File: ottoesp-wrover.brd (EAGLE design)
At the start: 57.2 x 53.3 mm, 43 parts, among them CN1 Servo, CN2 Servo, CN3 Servo, CN4 Servo, CN5 Servo, CN6 Servo, J1 DC-005, J2 4p-2.54, J3 4p-2.54, Q1 S8050, Q2 S8050, Q3 CJ2302, U1 CJT1117-5.0-SOT223, U2 CP2102, U3 CJA1117B-3.3-SOT89, U4 TPD4S012DRYR

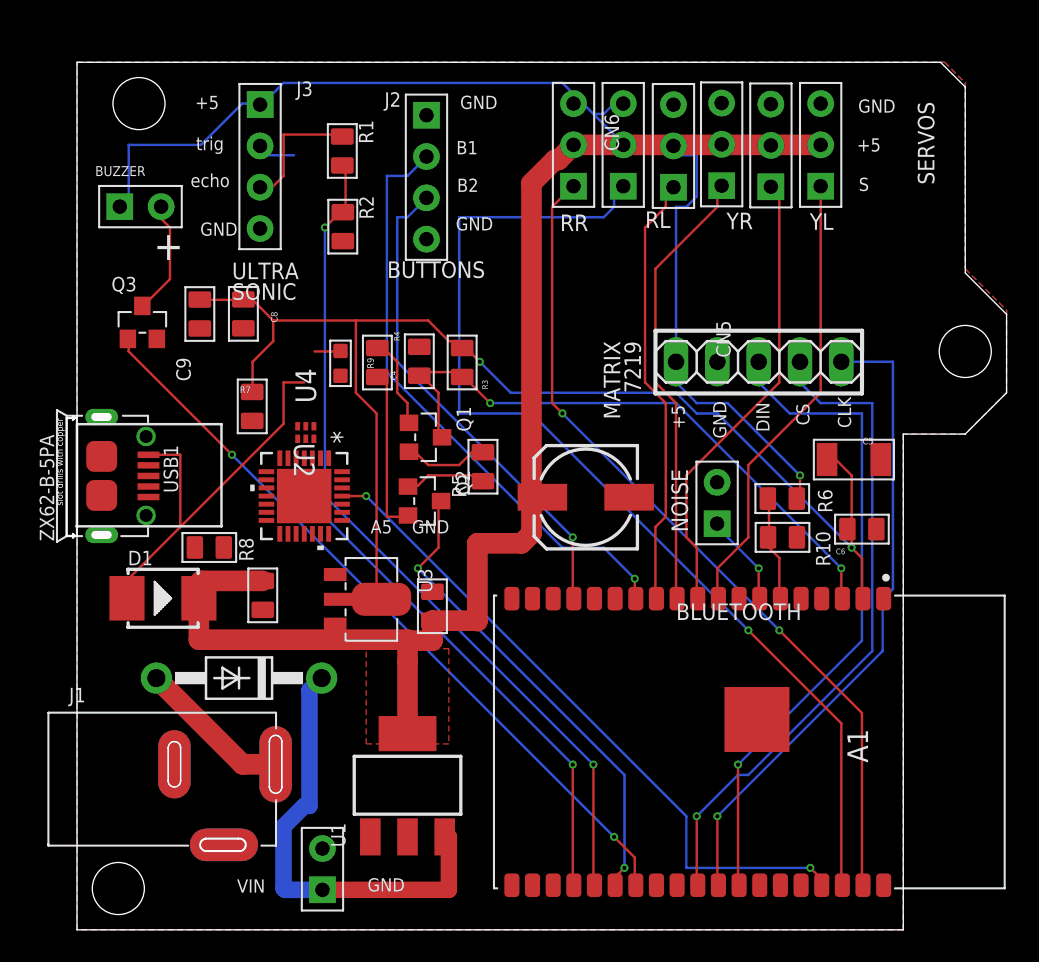
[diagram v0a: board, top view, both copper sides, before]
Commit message: Moved pins to allow a better PCB routing. Fixed all DRC errors.
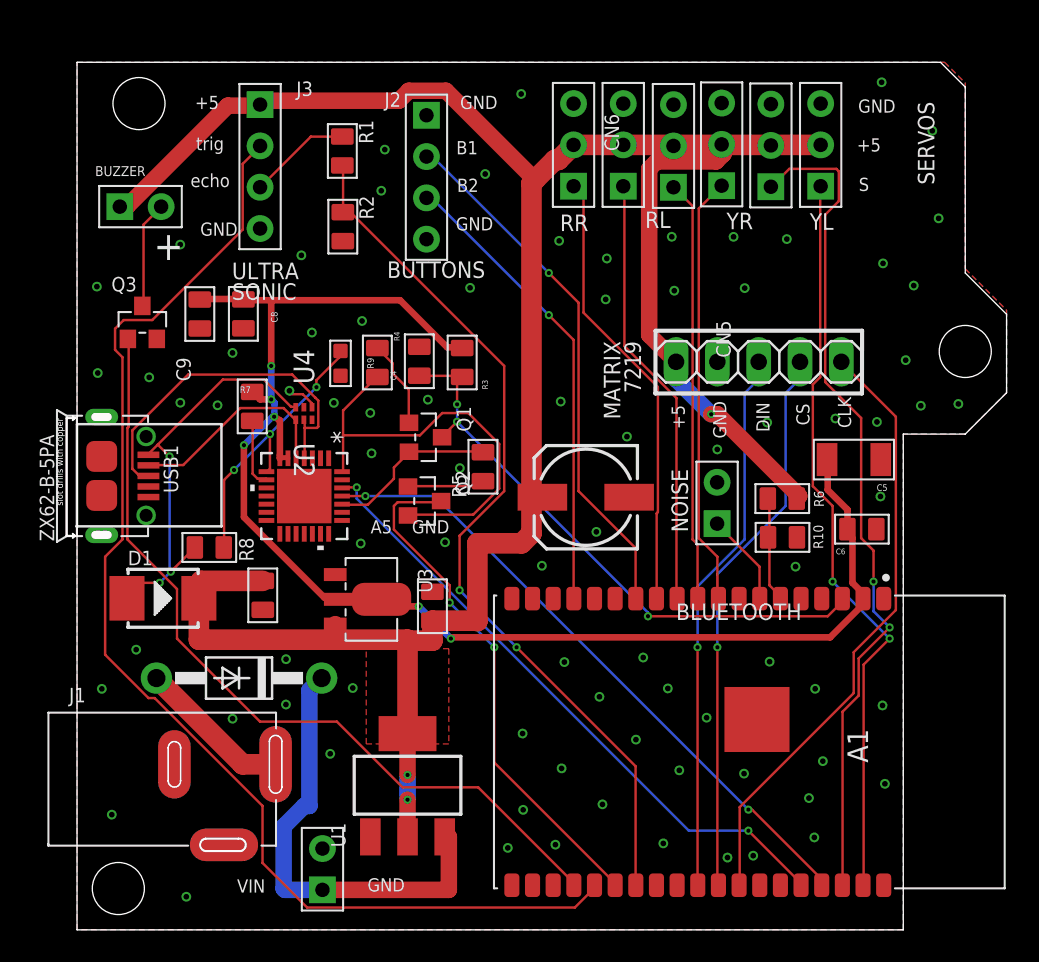
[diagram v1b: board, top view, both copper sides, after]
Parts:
- moved U4 1.17 mm to (24.1, 31.7)
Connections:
- net IO0 renamed BOOT
- net N$1 renamed RXD
- net N$2 renamed TXD
- net BUZZER: now also A1.23; no longer A1.26
- net CLK: now also A1.31; no longer A1.30
- net CS: now also A1.30; no longer A1.29
- net DIN: now also A1.29; no longer A1.31
- net ECHO3.3: now also A1.26; no longer A1.24
- net GND: now also CN5.3, CN6.3, U2.1, U2.2
- net SERVO1: now also A1.37; no longer A1.9
- net SERVO2: now also A1.36; no longer A1.10
- net SERVO3: now also A1.9; no longer A1.11
- net SERVO4: now also A1.10; no longer A1.12
- net SERVO5: now also A1.11; no longer A1.36
- net SERVO6: now also A1.12; no longer A1.37
- net TRIG: now also A1.24; no longer A1.23
- net V+: no longer CN5.3, CN6.3
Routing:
- net TRIG: track 34.2 -> 75.9 mm, vias 1 -> 0
- net RXD: track 0.00 -> 38.9 mm, vias 0 -> 2
- net SERVO5: track 65.0 -> 26.8 mm, vias 1 -> 0
- net SERVO6: track 51.4 -> 27.6 mm, vias 2 -> 0
- net SERVO2: track 28.2 -> 51.8 mm, vias 0 -> 2
- net N$10: track 0.00 -> 21.9 mm
- net SERVO1: track 28.0 -> 45.8 mm, vias 0 -> 2
- net DTR: track 10.3 -> 26.8 mm
- net N$7: track 1.60 -> 17.5 mm, vias 0 -> 3
- net N$8: track 0.00 -> 13.2 mm
- net 3.3V: track 82.0 -> 89.5 mm, vias 2 -> 6
- net DIN: track 40.6 -> 34.2 mm
- net RTS: track 5.69 -> 10.5 mm
- net CS: track 40.7 -> 36.1 mm
- net N$6: track 0.00 -> 4.29 mm
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
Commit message: Updated to use parts I can find at mouser. Used a higher power 3.3V regulator. Added Gerber zip that I used to order prototype boards from SEEED.
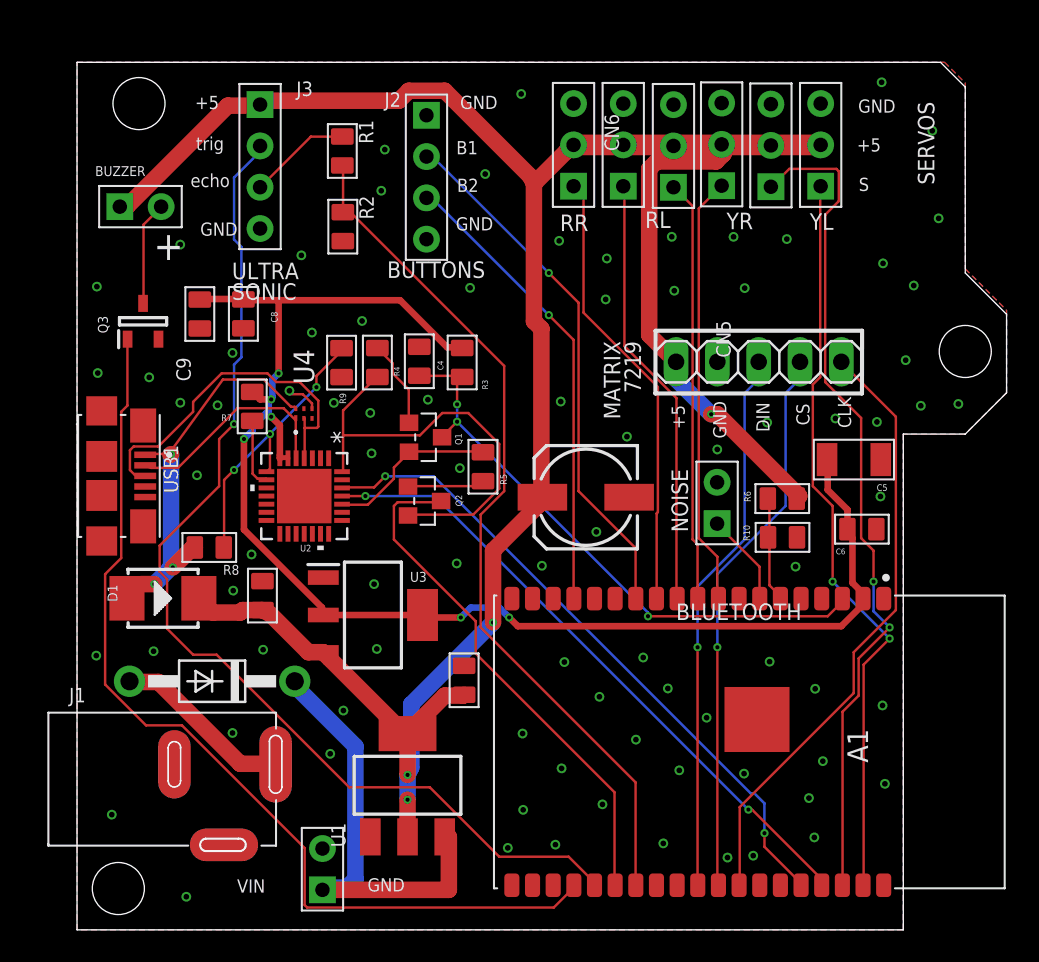
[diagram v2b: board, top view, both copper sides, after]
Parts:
- added FRAME1: FRAME-LEDGERMISHAFARMS, SparkFun-Aesthetics:MISHAFARMS
- Q3: device Seeed-Transistor:SOT-23 -> SamacSys_Parts:SOT95P230X110-3N
- R9: device OPL_Resistor:R0603 -> OPL_Resistor:R0805
- U1: value CJT1117-5.0-SOT223 -> 5.0V REG
- U3: device OPL_IC:SOT-89 -> SamacSys_Parts:SOT230P700X180-4N
- U4: device TPD4S012:DRY6 -> SamacSys_Parts:TPD4S012DRYR
- USB1: device OPL_Connector:MICRO-USB5+6P-SMD-0.65-AB -> XLibrary:HRS_ZX62-B-5PA(33)
- moved C1 4.95 mm to (34.0, 15.3)
- moved DP1 1.67 mm to (18.5, 15.3)
- moved U3 1.05 mm to (28.4, 19.4), turned to 0 degrees
- moved Q3 0.08 mm to (14.2, 37.4), turned to 90 degrees
- moved R9 0.08 mm to (26.4, 34.9)
- turned C3 to 180 degrees
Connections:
- net VBUS renamed N$1
- net GND: now also USB1.SH1, USB1.SH2, USB1.SH3, USB1.SH4, USB1.SH5, USB1.SH6; no longer USB1.P1, USB1.P2, USB1.P3, USB1.P4, USB1.P5, USB1.P6
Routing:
- net TRIG: track 75.9 -> 65.8 mm, vias 0 -> 1
- net BUZZER: track 50.5 -> 59.0 mm
- net V+: track 150.7 -> 147.5 mm, vias 3 -> 4
- net RXD: track 38.9 -> 40.6 mm
- net N$9: track 9.53 -> 11.1 mm
- net ECHO3.3: track 54.3 -> 53.3 mm, vias 2 -> 0
- net 3.3V: track 89.5 -> 90.2 mm
- net N$10: track 21.9 -> 22.5 mm
- net GND: track 2.07 -> 2.16 mm, vias 82 -> 85
- net BOOT: vias 2 -> 0
- removed copper zone on layer 1, net V+
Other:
- board text removed: "A5"

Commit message: .gitignore all the files that eagle creates that we don't want uploaded. Added the BOM in CSV (this is the BOM from Mouser) Changed a 20K resistor to 22K so that we don't need some many different resistors
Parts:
- R2: value 20K -> 22K
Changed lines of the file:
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@@
 <attribute name="VALUE" x="24.565678125" y="49.790540625" size="0.889" layer="27" ratio="11" rot="R270"/>
 </element>
-<element name="R2" library="OPL_Resistor" library_urn="urn:adsk.eagle:library:8004883" package="R0805" package3d_urn="urn:adsk.eagle:package:8004935/1" value="20K" x="26.500446875" y="43.233915625" smashed="yes" rot="R180">
+<element name="R2" library="OPL_Resistor" library_urn="urn:adsk.eagle:library:8004883" package="R0805" package3d_urn="urn:adsk.eagle:package:8004935/1" value="22K" x="26.500446875" y="43.233915625" smashed="yes" rot="R180">
 <attribute name="MPN" value="RC0805JR-071KL" x="26.500446875" y="43.233915625" size="1.778" layer="27" rot="R180" display="off"/>
 <attribute name="NAME" x="27.516446875" y="45.138915625" size="0.889" layer="25" ratio="11" rot="R270"/>

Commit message: The latest schematic and board layout
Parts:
- removed CN1, CN2, CN3, CN4, CN5, CN6: Servo, OPL_Connector:H3-2.54
- removed DP1: 1N4004, adafruit:DO41-10
- removed J2: 4p-2.54, OPL_Connector:H4-2.54
- removed JP4: 2p-2.54, OPL_Connector:H2-2.54
- removed U1: 5.0V REG, Seeed-IC:SOT-223
- added D2: PMEG3050EP,115, SamacSys_Parts:PMEG3050EP115
- added JP1: PINHD-2X6, Connector:2X06
- added LA, LF, LL, RA, RF, RL: Servo, OPL_Connector:H3-2.54
- D1: value 28V-5A -> PMEG3050EP,115; device Seeed-Diode:DO-214AA -> SamacSys_Parts:PMEG3050EP115
- moved JP3 42.4 mm to (27.5, 4.24), turned to 0 degrees
- moved JP2 42.2 mm to (13.8, 44.4)
- moved JP6 40.7 mm to (21.8, 7.67), turned to 90 degrees
- moved Q3 38.7 mm to (32.7, 3.43), turned to 180 degrees
- moved USB1 37.5 mm to (40.6, 51.8), turned to 180 degrees
- moved R1 35.5 mm to (32.4, 12.9)
- moved J3 35.1 mm to (27.5, 12.4), turned to 180 degrees
- moved R2 34.8 mm to (32.4, 8.90)
- moved J1 34.3 mm to (22.9, 44.3), turned to 270 degrees
- moved C3 29.9 mm to (27.9, 49.8)
- moved C4 27.7 mm to (58.6, 30.9), turned to 90 degrees
- moved R8 27.4 mm to (34.3, 45.8), turned to 0 degrees
- moved R4 26.1 mm to (54.6, 31.8), turned to 270 degrees
- moved D1 26.0 mm to (31.8, 40.6)
- moved U4 25.1 mm to (45.7, 44.4), turned to 180 degrees
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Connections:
- net N$10 renamed D+
- net N$8 renamed D-
- removed net N$1: D1.+, R8.1, U4.6, USB1.1
- removed net N$9: DP1.A, J1.+
- new net GPIO12: A1.14, JP1.2
- new net GPIO21: A1.33, JP1.4
- new net GPIO32: A1.8, JP1.6
- new net USBV+: D1.2, R8.1, U4.6, USB1.1
- net 3.3V: now also C2.+
- net BUTTON1: now also JP1.8; no longer J2.2
- net BUTTON2: now also JP1.10; no longer J2.3
- net GND: now also JP1.1, JP1.11, JP1.3, JP1.5, JP1.7, JP1.9, LA.3, LF.3, LL.3, RA.3, RF.3, RL.3; no longer CN1.3, CN2.3, CN3.3, CN4.3, CN5.3, CN6.3, J2.1, J2.4, JP4.2, U1.1
- net N$11: now also D2.2; no longer DP1.C, U1.3
- net NOISE: now also JP1.12; no longer JP4.1
- net SERVO1: now also LL.1; no longer CN1.1
- net SERVO2: now also RL.1; no longer CN2.1
- net SERVO3: now also LF.1; no longer CN3.1
- net SERVO4: now also RF.1; no longer CN4.1
- net SERVO5: now also LA.1; no longer CN5.1
- net SERVO6: now also RA.1; no longer CN6.1
- net V+: now also D1.1, D2.1, J1.+, LA.2, LF.2, LL.2, RA.2, RF.2, RL.2; no longer C2.+, CN1.2, CN2.2, CN3.2, CN4.2, CN5.2, CN6.2, D1.-, U1.2, U1.TER
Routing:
- net GPIO21: track 0.00 -> 65.9 mm, vias 0 -> 1
- net BUZZER: track 59.0 -> 7.74 mm
- net TRIG: track 65.8 -> 18.1 mm, vias 1 -> 0
- net GPIO32: track 0.00 -> 37.5 mm, vias 0 -> 2
- net ECHO3.3: track 53.3 -> 17.5 mm, vias 0 -> 2
- net NOISE: track 5.90 -> 39.6 mm, vias 0 -> 2
- net GPIO12: track 0.00 -> 30.4 mm
- net N$1: track 25.4 -> 0.00 mm, vias 3 -> 0
- net USBV+: track 0.00 -> 24.3 mm, vias 0 -> 3
- net N$11: track 27.3 -> 5.92 mm
- net EN: track 37.0 -> 22.7 mm, vias 3 -> 2
- net SERVO2: track 51.8 -> 39.1 mm, vias 2 -> 3
- net SERVO6: track 27.6 -> 40.2 mm, vias 0 -> 1
- net RTS: track 10.5 -> 22.8 mm
- net N$9: track 11.1 -> 0.00 mm
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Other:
- board text added: "12"
- board text added: "21"
- board text added: "32"
- board text added: "BTN1"
- board text added: "BTN2"
- board text added: "Battery"
- board text added: "Buzzer"
- board text added: "Echo"
- board text added: "Noise"
- board text added: "Trig"
- board text added: "V+"
- board text removed: "+5"
- board text removed: "7219"
- board text removed: "B1"
- board text removed: "B2"
- board text removed: "BLUETOOTH"
- board text removed: "BUTTONS"
- board text removed: "BUZZER"
- board text removed: "MATRIX"
- board text removed: "NOISE"
- board text removed: "RL"
- board text removed: "RR"
- board text removed: "S"
- board text removed: "SERVOS"
- board text removed: "SONIC"
- board text removed: "ULTRA"
- board text removed: "VIN"
- board text removed: "YL"
- board text removed: "YR"
- board text removed: "echo"
- board text removed: "trig"

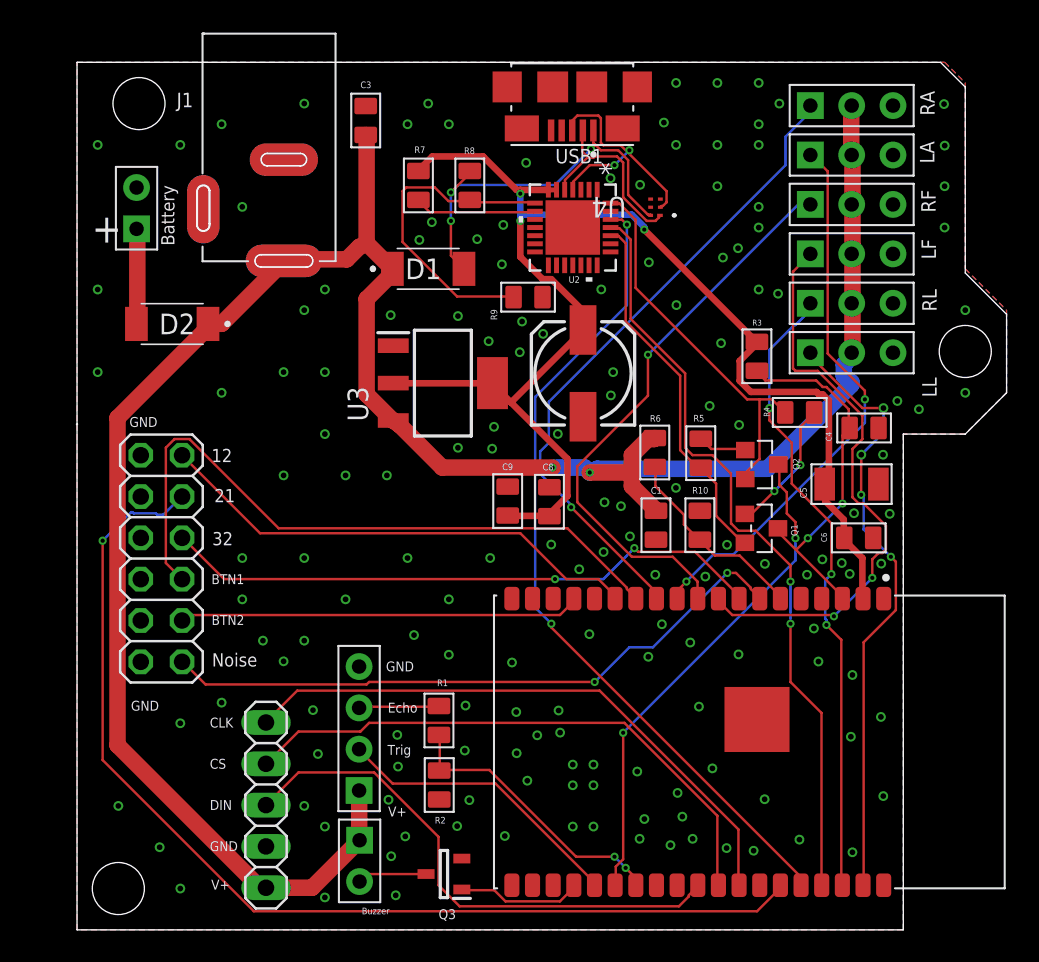
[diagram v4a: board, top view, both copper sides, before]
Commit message: Added pins with V+, 3.3V, and GND for expansion
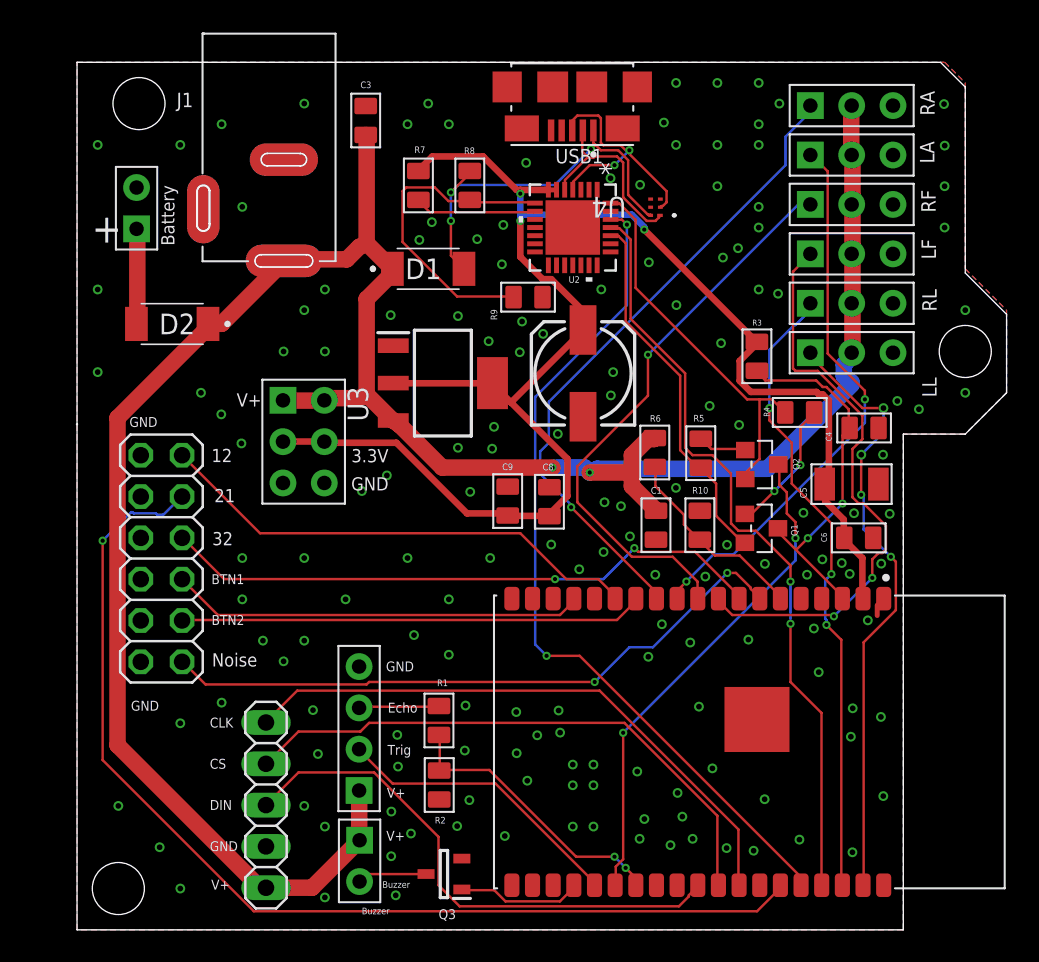
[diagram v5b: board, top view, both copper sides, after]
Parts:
- added J2: 2x3p-2.54, OPL_Connector:H2X3-2.54
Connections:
- net 3.3V: now also J2.2, J2.5
- net BUTTON1: now also JP1.10; no longer JP1.8
- net BUTTON2: now also JP1.8; no longer JP1.10
- net GND: now also J2.3, J2.4
- net V+: now also J2.1, J2.6
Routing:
- net 3.3V: track 85.7 -> 101.4 mm
- net BUTTON1: track 41.7 -> 28.5 mm
- net V+: track 140.1 -> 145.3 mm
- net RXD: track 50.9 -> 52.1 mm
- net BUTTON2: track 24.7 -> 25.5 mm
- net GND: track 0.00 -> 0.64 mm, vias 159 -> 160
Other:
- board text added: "3.3V"
